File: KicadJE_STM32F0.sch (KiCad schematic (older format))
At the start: 101 parts, among them J401 CV1, J402 CV2, J403 OUT1, J404 OUT2, J405 OUT3, J406 OUT4, J407 IN1, J408 IN2, J409 I2C, P401 Doepfer_Power_16pin, SW401 SW_SPDT, U401 TL072, U402 TL072, U405 MCP4822

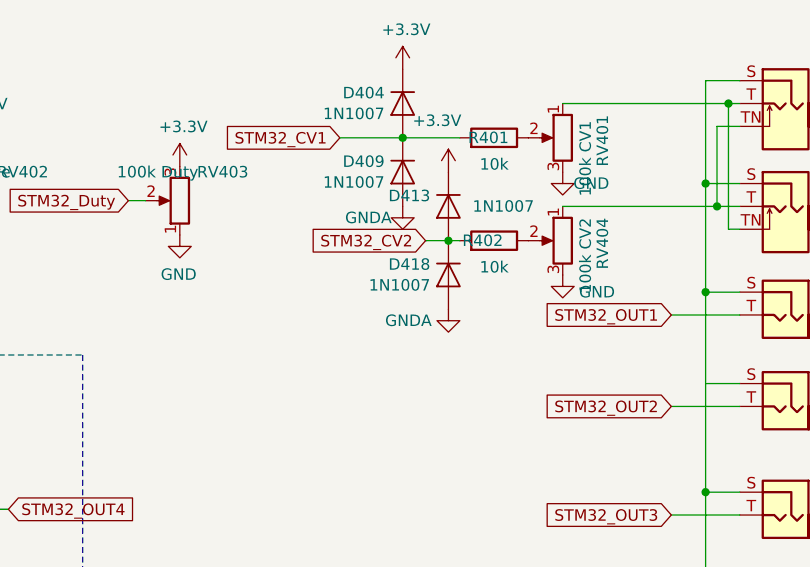
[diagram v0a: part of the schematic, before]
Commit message: Diode protection - STM32
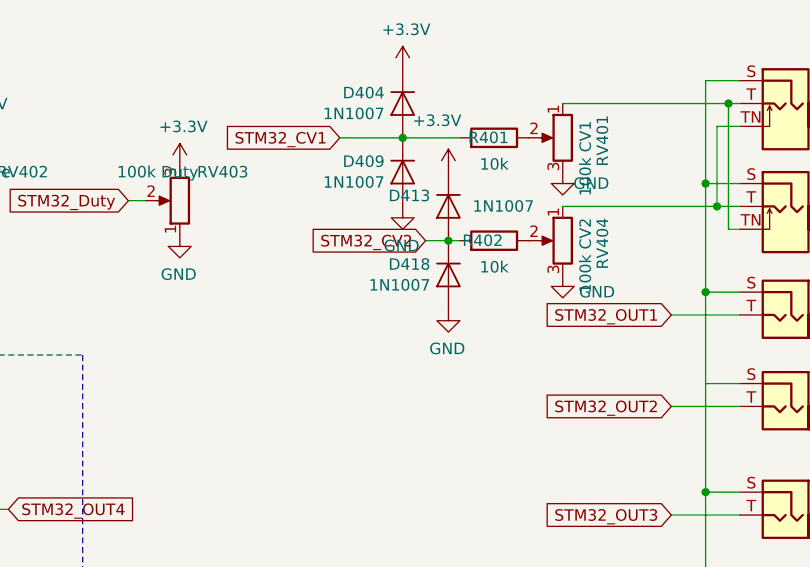
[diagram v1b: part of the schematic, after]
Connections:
- net GND: now also D409.2 (A), D418.2 (A)
- net GNDA: no longer D409.2 (A), D418.2 (A)
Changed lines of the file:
@@
 	10325 3375 10325 3825
-$Comp
-L power:GNDA #PWR?
-U 1 1 5CE656C0
-P 9000 1225
-AR Path="/5CE656C0" Ref="#PWR?"  Part="1"
-AR Path="/5CD3F059/5CE656C0" Ref="#PWR?"  Part="1"
-AR Path="/5CE53731/5CE656C0" Ref="#PWR0412"  Part="1"
-F 0 "#PWR0412" H 9000 975 50  0001 C CNN
-F 1 "GNDA" H 9150 1175 50  0000 C CNN
-F 2 "" H 9000 1225 50  0001 C CNN
-F 3 "" H 9000 1225 50  0001 C CNN
-	1    9000 1225
-	-1   0    0    -1
-$EndComp
 $Comp
 L Amplifier_Operational:TL072 U?
@@
 	1    9400 1375
 	0    1    -1   0
-$EndComp
-$Comp
-L power:GNDA #PWR?
-U 1 1 5CE6578E
-P 9200 1675
-AR Path="/5CE6578E" Ref="#PWR?"  Part="1"
-AR Path="/5CD3F059/5CE6578E" Ref="#PWR?"  Part="1"
-AR Path="/5CE53731/5CE6578E" Ref="#PWR0421"  Part="1"
-F 0 "#PWR0421" H 9200 1425 50  0001 C CNN
-F 1 "GNDA" H 9375 1625 50  0000 C CNN
-F 2 "" H 9200 1675 50  0001 C CNN
-F 3 "" H 9200 1675 50  0001 C CNN
-	1    9200 1675
-	-1   0    0    -1
 $EndComp
 $Comp
@@
 Text GLabel 6175 1600 3    39   Input ~ 0
 PA15_C2
+$Comp
+L Envelope-cache-2018-08-04-13-00-04:GND #PWR?
+U 1 1 5DB28C50
+P 9200 1675
+AR Path="/5DB28C50" Ref="#PWR?"  Part="1"
+AR Path="/5CE53731/5DB28C50" Ref="#PWR0106"  Part="1"
+F 0 "#PWR0106" H 9200 1425 50  0001 C CNN
+F 1 "GND" H 9205 1502 50  0000 C CNN
+F 2 "" H 9200 1675 50  0001 C CNN
+F 3 "" H 9200 1675 50  0001 C CNN
+	1    9200 1675
+	-1   0    0    -1
+$EndComp
+$Comp
+L Envelope-cache-2018-08-04-13-00-04:GND #PWR?
+U 1 1 5DB5255D
+P 9000 1225
+AR Path="/5DB5255D" Ref="#PWR?"  Part="1"
+AR Path="/5CE53731/5DB5255D" Ref="#PWR?"  Part="1"
+F 0 "#PWR?" H 9000 975 50  0001 C CNN
+F 1 "GND" H 9005 1052 50  0000 C CNN
+F 2 "" H 9000 1225 50  0001 C CNN
+F 3 "" H 9000 1225 50  0001 C CNN
+	1    9000 1225
+	-1   0    0    -1
+$EndComp
 $EndSCHEMATC

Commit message: Diode etc
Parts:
- removed D401, D402, D405, D406, D407, D410, D411, D412, D415, D416, D417: LED, LED_THT:LED_D3.0mm, symbol Device:LED
- removed R429, R430, R431, R432, R433, R434: 100R, Resistor_SMD:R_0805_2012Metric_Pad1.15x1.40mm_HandSolder, symbol Device:R_Small
- R437: value 100R -> 820R
- renumbered D403 to D401
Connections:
- net GND: now also D401.1 (K)
- net PA15_C2: no longer D401.1 (K), R437.2
- net PB0_R0: no longer D401.2 (A)
- net at R437.1: now also D401.2 (A)
- net STM32F103C8/STM32_SDA1_PWM_PB9 renamed PB9_PWM
- net PB9_PWM: now also R437.2
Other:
- moved on the sheet: D401, JP407, R437

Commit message: ERC Performed
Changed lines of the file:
@@
 Wire Wire Line
 	2950 1425 2825 1425
-$Comp
-L power:PWR_FLAG #FLG?
-U 1 1 5CE76D20
-P 2825 825
-AR Path="/5CD3F059/5CE76D20" Ref="#FLG?"  Part="1"
-AR Path="/5CE76D20" Ref="#FLG?"  Part="1"
-AR Path="/5CE53731/5CE76D20" Ref="#FLG0401"  Part="1"
-F 0 "#FLG0401" H 2825 900 50  0001 C CNN
-F 1 "PWR_FLAG" H 2825 998 50  0000 C CNN
-F 2 "" H 2825 825 50  0001 C CNN
-F 3 "~" H 2825 825 50  0001 C CNN
-	1    2825 825
-	1    0    0    -1
-$EndComp
 Connection ~ 2825 825
-$Comp
-L power:PWR_FLAG #FLG?
-U 1 1 5CE76D27
-P 2825 1425
-AR Path="/5CD3F059/5CE76D27" Ref="#FLG?"  Part="1"
-AR Path="/5CE76D27" Ref="#FLG?"  Part="1"
-AR Path="/5CE53731/5CE76D27" Ref="#FLG0402"  Part="1"
-F 0 "#FLG0402" H 2825 1500 50  0001 C CNN
-F 1 "PWR_FLAG" H 2825 1598 50  0000 C CNN
-F 2 "" H 2825 1425 50  0001 C CNN
-F 3 "~" H 2825 1425 50  0001 C CNN
-	1    2825 1425
-	-1   0    0    1
-$EndComp
 Connection ~ 2825 1425
 $Comp
